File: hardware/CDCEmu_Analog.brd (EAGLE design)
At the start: 60 x 40 mm, 72 parts, among them J1 Audio In, J2 Audio Out, J3 Mic In, Q1 PCH, Q10 NPN, Q2 NCH, Q3 NCH, Q4 PCH, Q5 NCH, Q6 NPN, Q7 NPN, Q8 NPN, Q9 NPN, U1 1117, U2 BK8000L, U3 LM358, U4 NE5532

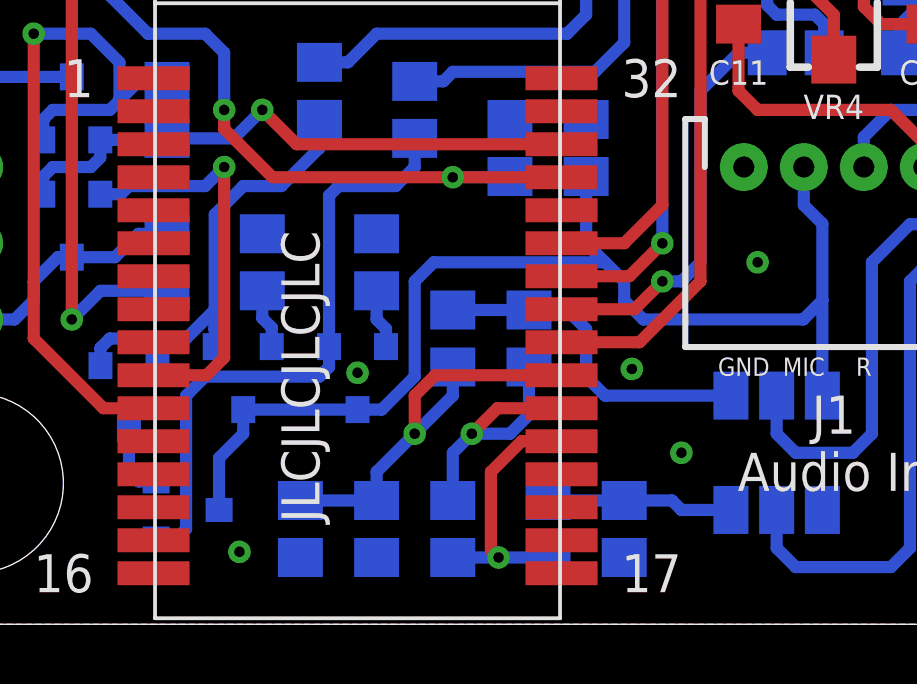
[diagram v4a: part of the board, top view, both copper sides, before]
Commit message: [HW/Analog] Correct Vol+/- control transistors
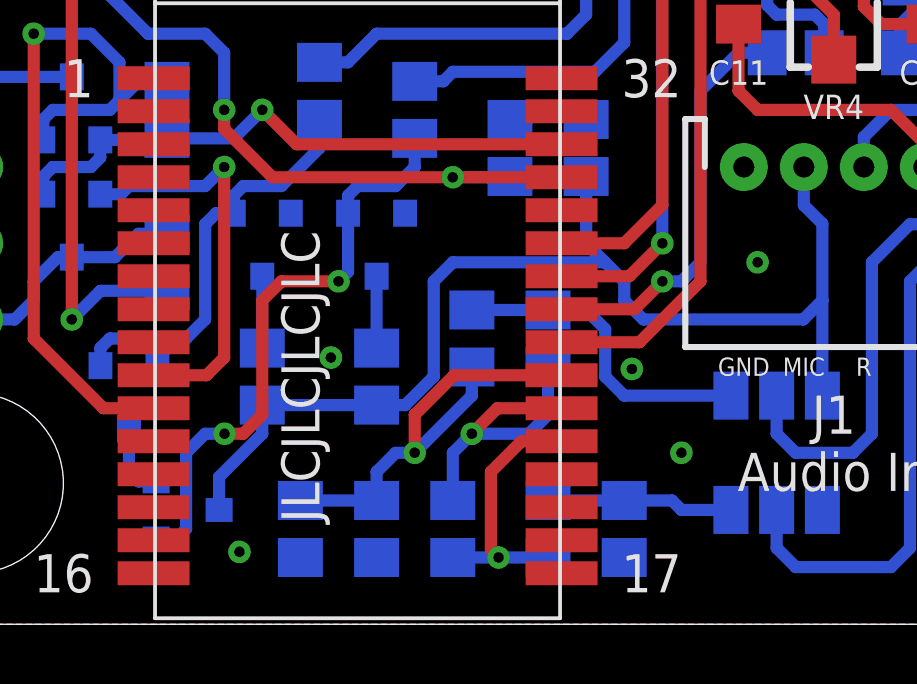
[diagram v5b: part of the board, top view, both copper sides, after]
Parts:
- moved Q9 4.49 mm to (14.6, 12.7)
- moved Q8 4.49 mm to (18.4, 12.7)
- moved R19 3.81 mm to (18.4, 8.26)
- moved R20 3.81 mm to (14.6, 8.26)
- moved R24 0.64 mm to (21.6, 9.53)
- moved C17 0.63 mm to (24.1, 9.53)
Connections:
- removed net Q7E: Q8.2, R19.2
- removed net Q8E: Q9.2, R20.2
- new net Q8C: Q8.3, R19.1
- new net Q9C: Q9.3, R20.1
- net CTRL: now also R19.2, R20.2; no longer Q8.3, Q9.3
- net GND: now also Q8.2, Q9.2; no longer R19.1, R20.1
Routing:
- net Q9C: track 0.00 -> 2.39 mm
- net Q8C: track 0.00 -> 2.39 mm
- net Q7E: track 1.99 -> 0.00 mm
- net Q8E: track 1.99 -> 0.00 mm
- net P7B: track 15.3 -> 13.8 mm
- net VMIC: track 14.5 -> 15.7 mm
- net P3B: track 20.7 -> 19.9 mm, vias 0 -> 2
- net BT_MICP: track 11.4 -> 10.7 mm
- net MIC_P: track 9.59 -> 10.2 mm
